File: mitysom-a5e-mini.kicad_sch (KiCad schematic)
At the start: 26 parts, among them J201 Plug_Samtec_SEAM-50-02.0-L-08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, J202 PinHeader_1x3_P2.54mm_Drill1.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, J203 Socket_Samtec_ERF8_2x20_ERF8-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

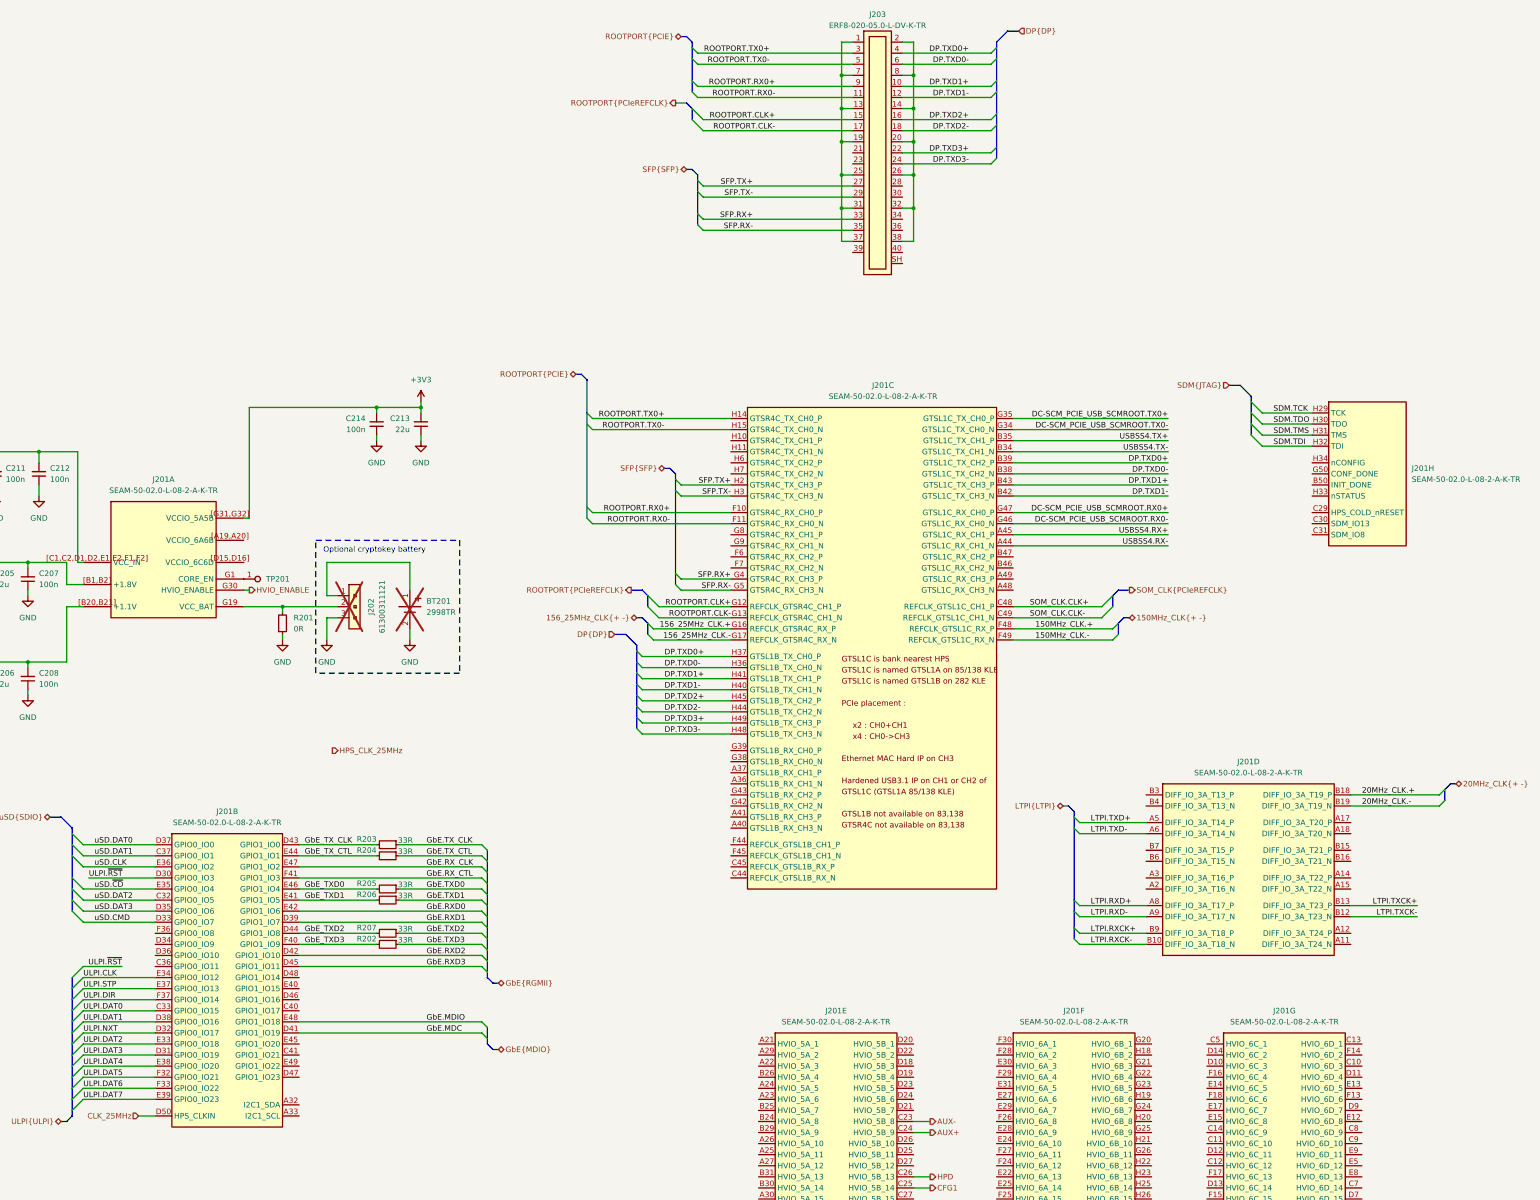
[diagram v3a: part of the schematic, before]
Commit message: [#100060] Move high speed connector to separate schematic sheet, connect it to SoM
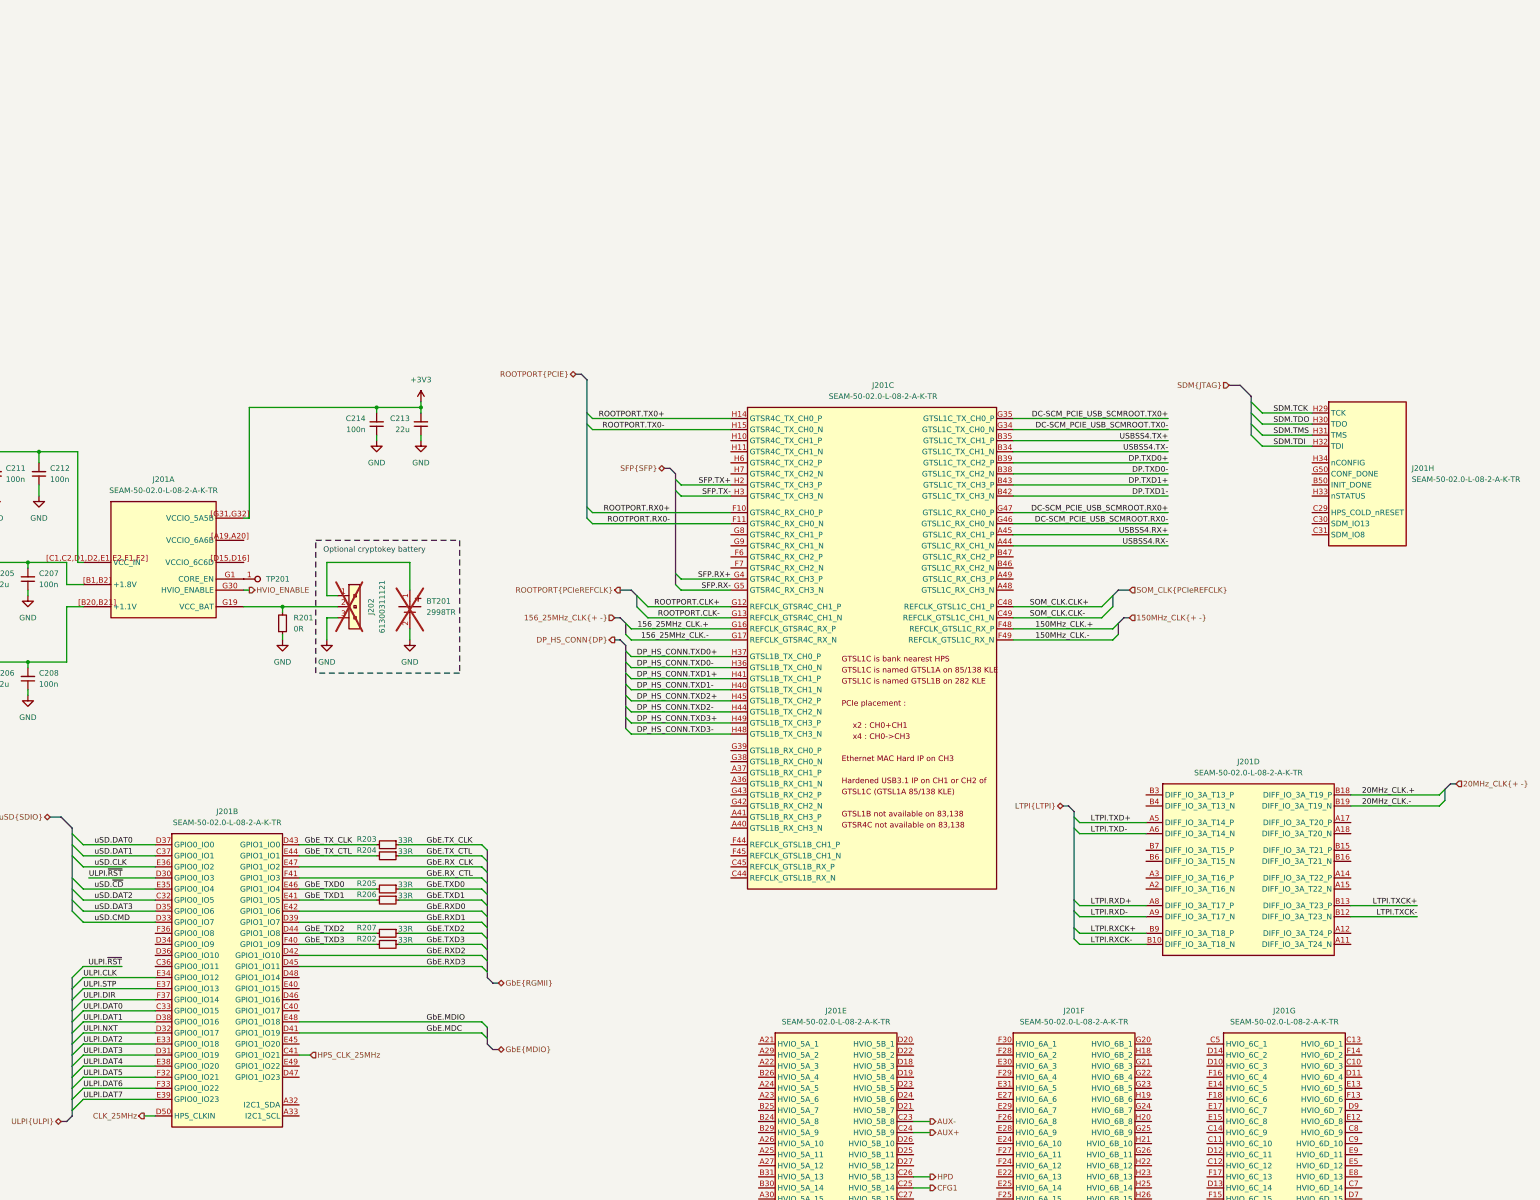
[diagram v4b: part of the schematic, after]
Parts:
- removed J203: Socket_Samtec_ERF8_2x20_ERF8-020-05.0-L-DV-K-TR, antmicro-footprints:Conn_Socket_Samtec_ERF8_2x20_ERF8-020-05.0-L-DV-K-TR, symbol antmicroB2BConnectors:Socket_Samtec_ERF8_2x20_ERF8-020-05.0-L-DV-K-TR
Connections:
- net DP.TXD0+: no longer J201.H37 (GTSL1B_TX_CH0_P)
- net DP.TXD0-: no longer J201.H36 (GTSL1B_TX_CH0_N)
- net DP.TXD1+: no longer J201.H41 (GTSL1B_TX_CH1_P)
- net DP.TXD1-: no longer J201.H40 (GTSL1B_TX_CH1_N)
- net HPS_CLK_25MHz: now also J201.C41 (GPIO1_IO21)
- net DP.TXD2+ renamed DP_HS_CONN.TXD2+
- net DP.TXD2- renamed DP_HS_CONN.TXD2-
- net DP.TXD3+ renamed DP_HS_CONN.TXD3+
- net DP.TXD3- renamed DP_HS_CONN.TXD3-
- new net DP_HS_CONN.TXD0+: J201.H37 (GTSL1B_TX_CH0_P)
- new net DP_HS_CONN.TXD0-: J201.H36 (GTSL1B_TX_CH0_N)
- new net DP_HS_CONN.TXD1+: J201.H41 (GTSL1B_TX_CH1_P)
- new net DP_HS_CONN.TXD1-: J201.H40 (GTSL1B_TX_CH1_N)

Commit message: [#100060] Fix SoM DP and PCIe bus naming
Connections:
- net DC-SCM_PCIE_USB_SCMROOT.RX0+ renamed SOM_PCIE_DEVICE.RX0+
- net DC-SCM_PCIE_USB_SCMROOT.RX0- renamed SOM_PCIE_DEVICE.RX0-
- net DC-SCM_PCIE_USB_SCMROOT.TX0+ renamed SOM_PCIE_DEVICE.TX0+
- net DC-SCM_PCIE_USB_SCMROOT.TX0- renamed SOM_PCIE_DEVICE.TX0-

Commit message: [#100125] Add misc schematic sheet, connect buttons
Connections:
- net ~{RESET_BTN}: now reaches J201.C29 (HPS_COLD_nRESET)
- net ~{CONFIG_BTN}: now reaches J201.H34 (nCONFIG)
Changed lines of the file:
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@@
 		)
 	)
+	(wire
+		(pts
+			(xy 372.11 38.1) (xy 375.92 38.1)
+		)
+		(stroke
+			(width 0)
+			(type default)
+		)
+	)
 	(bus
 		(pts
@@
 	(wire
 		(pts
+			(xy 372.11 49.53) (xy 375.92 49.53)
+		)
+		(stroke
+			(width 0)
+			(type default)
+		)
+	)
+	(wire
+		(pts
 			(xy 31.75 245.11) (xy 34.29 245.11)
 		)
@@
 	)
 	(hierarchical_label "DP{DP}"
-		(shape input)
+		(shape output)
 		(at 262.89 227.33 0)
 		(effects
@@
 		)
 	)
+	(hierarchical_label "~{RESET_BTN}"
+		(shape input)
+		(at 372.11 49.53 180)
+		(effects
+			(font
+				(size 1.27 1.27)
+			)
+			(justify right)
+		)
+	)
 	(hierarchical_label "LTPI{LTPI}"
 		(shape bidirectional)
@@
 		)
 	)
+	(hierarchical_label "~{CONFIG_BTN}"
+		(shape input)
+		(at 372.11 38.1 180)
+		(effects
+			(font
+				(size 1.27 1.27)
+			)
+			(justify right)
+		)
+	)
 	(hierarchical_label "AUX_DRV_OUT"
 		(shape input)
@@
 		(effects
 			(font
+				(size 1.27 1.27)
+			)
+			(justify right)
+		)
+	)
+	(hierarchical_label "~{USER_BTN}"
+		(shape input)
+		(at 372.11 64.77 180)
+		(effects
+			(font

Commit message: [#100092] Connect eSPI to MitySOM. Supply 6A and 6B bank with 1V8
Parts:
- added C215: C_100n_0402, antmicro-footprints:C_0402_1005Metric, symbol antmicroCapacitors0402:C_100n_0402
- added C216: C_22u_10V_0402, antmicro-footprints:C_0402_1005Metric, symbol antmicroCapacitors0402:C_22u_10V_0402
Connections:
- net +1V8: now also J201.[A19,A20] (VCCIO_6A6B), C215.2, C216.2
- net GND: now also C215.1, C216.1
- net DC_SCM_ESPI.IO2: now reaches J201.E27 (HVIO_6A_6)
- net DC_SCM_ESPI.SCK: now reaches J201.E28 (HVIO_6A_9)
- net DC_SCM_ESPI.IO3: now reaches J201.E29 (HVIO_6A_7)
- net DC_SCM_ESPI.~{RESET}: now reaches J201.E30 (HVIO_6A_3)
- net DC_SCM_ESPI.IO1: now reaches J201.E31 (HVIO_6A_5)
- net DC_SCM_ESPI.~{ALERT0}: now reaches J201.F26 (HVIO_6A_8)
- net DC_SCM_ESPI.~{CS0}: now reaches J201.F28 (HVIO_6A_2)
- net DC_SCM_ESPI.IO0: now reaches J201.F29 (HVIO_6A_4)
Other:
- moved on the sheet: C213, C214, J201E, J201F

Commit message: [#99649] Connect low-speed and control signals to MitySOM.
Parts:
- added C217: C_100n_0402, antmicro-footprints:C_0402_1005Metric, symbol antmicroCapacitors0402:C_100n_0402
- added C218: C_22u_10V_0402, antmicro-footprints:C_0402_1005Metric, symbol antmicroCapacitors0402:C_22u_10V_0402
- added R208: R_240R_0402, antmicro-footprints:R_0402_1005Metric, symbol antmicroResistors0402:R_240R_0402
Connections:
- net GND: now also C217.1, C218.1, R208.1
- net LTPI.RXD+: now also J201.A12 (DIFF_IO_3A_T24_P); no longer J201.A8 (DIFF_IO_3A_T17_P)
- net LTPI.RXD-: now also J201.A11 (DIFF_IO_3A_T24_N); no longer J201.A9 (DIFF_IO_3A_T17_N)
- net at J201.[D15,D16] (VCCIO_6C6D): now also C217.2, C218.2
- net FAN_EN: now reaches J201.D47 (GPIO1_IO23)
- net UART.TX: now reaches J201.D48 (GPIO1_IO14)
- net UART.RX: now reaches J201.E40 (GPIO1_IO15)
- net SFP_TX_FLT_3V3: now reaches J201.A25 (HVIO_5A_11)
- net SFP_TX_DIS_3V3: now reaches J201.A26 (HVIO_5A_10)
- net SFP_SDA_3V3: now reaches J201.A27 (HVIO_5A_12)
- net SFP_SCL_3V3: now reaches J201.A28 (HVIO_5A_16)
- net SFP_RS0_3V3: now reaches J201.A30 (HVIO_5A_15)
- net SFP_LOS_3V3: now reaches J201.B26 (HVIO_5A_4)
- net SFP_MOD0_PRSNT_N_3V3: now reaches J201.B29 (HVIO_5A_9)
- net ~{DEBUG1_BTN}: now reaches J201.C6 (HVIO_6D_17)
- net ~{DEBUG2_BTN}: now reaches J201.D5 (HVIO_6D_18)
- new net: J201.A8 (DIFF_IO_3A_T17_P), R208.2
- no-connect marks 0 -> 3
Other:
- note added: "ETH PHY RESET?"
- note added: "LEDs are on SOM"
- note added: "RZQ"
- moved on the sheet: C213, C214, C215, C216
